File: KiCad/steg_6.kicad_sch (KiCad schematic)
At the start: 13 parts, among them U5 W65C02S, U6 LCD

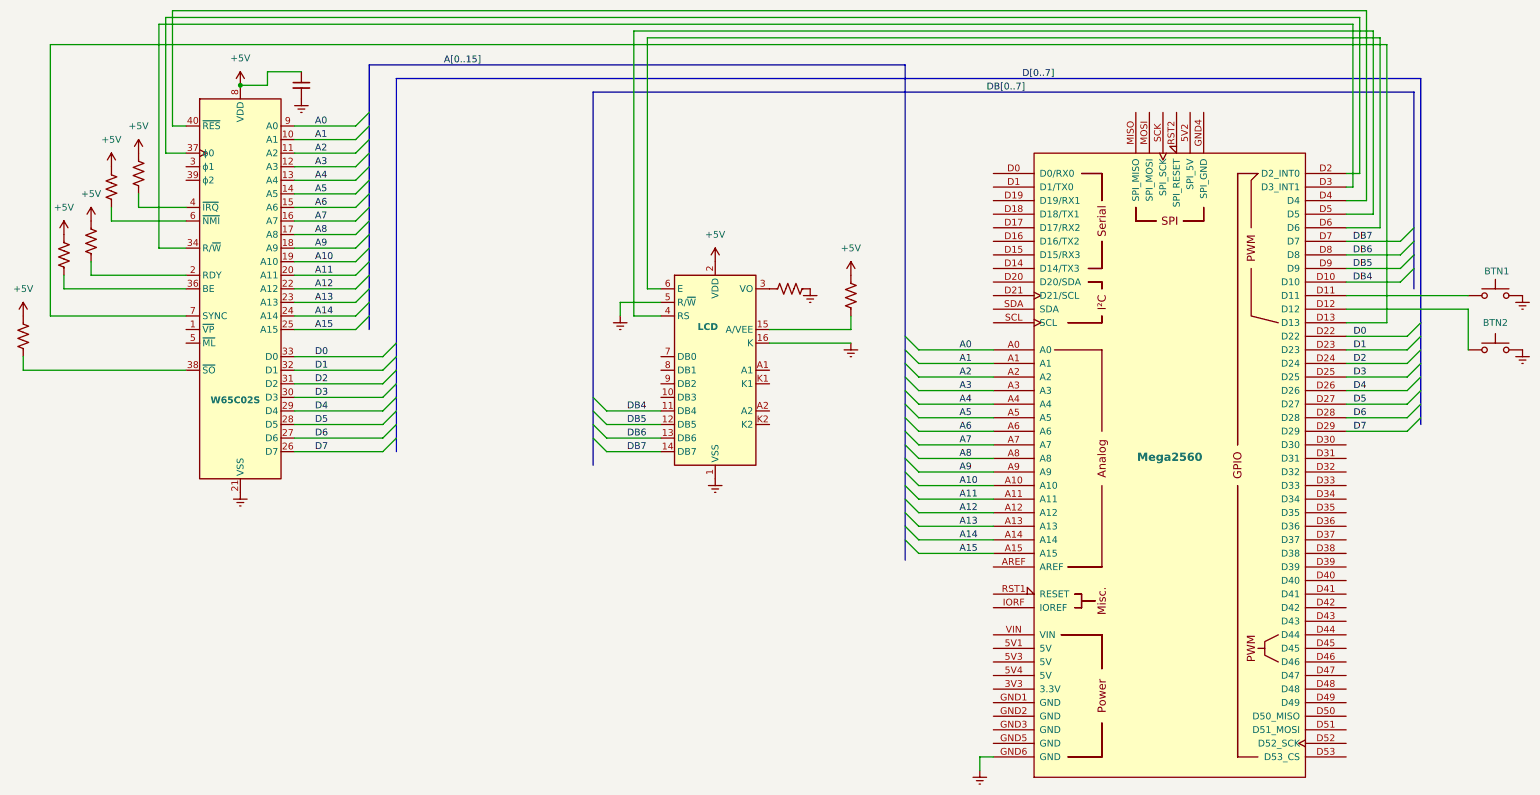
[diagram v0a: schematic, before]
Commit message: Add trim potentiometer symbol and update power symbols in schematics
- Introduced a new trim potentiometer symbol (Device:R_Potentiometer_Trim) with properties for reference, value, footprint, and simulation details.
- Updated existing power symbols for +5V and Earth, including new references and descriptions.
- Adjusted positions and properties of various components in the schematic to enhance clarity and organization.
- Updated multiple schematic images to reflect the latest changes.
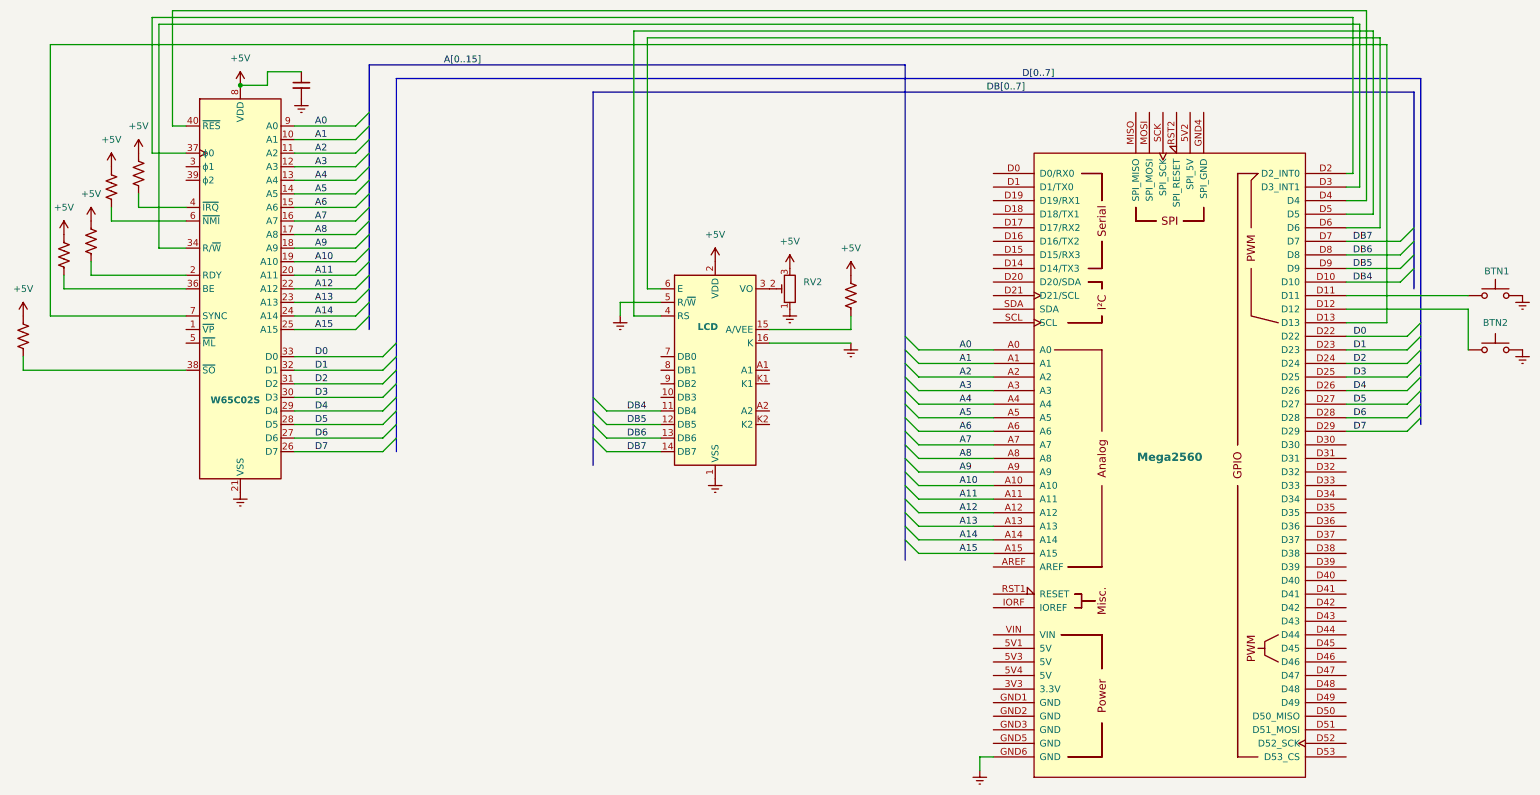
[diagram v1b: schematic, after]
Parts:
- removed R13: (no value), symbol Device:R_US
- added RV2: R_Potentiometer_Trim, symbol Device:R_Potentiometer_Trim
- R14: value (none) -> 220
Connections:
- net +5V: now also RV2.3
- net Earth: now also RV2.1
- net at U6.3 (VO): now also RV2.2
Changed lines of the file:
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@@
 	(wire
 		(pts
-			(xy 90.17 53.34) (xy 313.69 53.34)
+			(xy 87.63 53.34) (xy 312.42 53.34)
 		)
 		(stroke
@@
 	(wire
 		(pts
+			(xy 311.15 82.55) (xy 312.42 82.55)
+		)
+		(stroke
+			(width 0)
+			(type default)
+		)
+	)
+	(wire
+		(pts
 			(xy 175.26 106.68) (xy 182.88 106.68)
 		)
@@
 	(wire
 		(pts
-			(xy 88.9 54.61) (xy 312.42 54.61)
+			(xy 88.9 54.61) (xy 313.69 54.61)
 		)
 		(stroke
@@
 	(wire
 		(pts
-			(xy 90.17 53.34) (xy 90.17 78.74)
+			(xy 87.63 53.34) (xy 87.63 78.74)
 		)
 		(stroke
@@
 	(wire
 		(pts
-			(xy 90.17 78.74) (xy 93.98 78.74)
+			(xy 87.63 78.74) (xy 93.98 78.74)
 		)
 		(stroke
@@
 	(wire
 		(pts
-			(xy 312.42 85.09) (xy 311.15 85.09)
+			(xy 313.69 85.09) (xy 311.15 85.09)
 		)
 		(stroke
@@
 	(wire
 		(pts
-			(xy 312.42 54.61) (xy 312.42 85.09)
+			(xy 313.69 54.61) (xy 313.69 85.09)
 		)
 		(stroke
@@
 	(wire
 		(pts
-			(xy 313.69 53.34) (xy 313.69 82.55)
+			(xy 312.42 53.34) (xy 312.42 82.55)
 		)
 		(stroke
@@
 		(pts
 			(xy 93.98 96.52) (xy 88.9 96.52)
-		)
-		(stroke
-			(width 0)
-			(type default)
-		)
-	)
-	(wire
-		(pts
-			(xy 313.69 82.55) (xy 311.15 82.55)
 		)
 		(stroke
@@
 	)
 	(symbol
-		(lib_id "Device:R_US")
-		(at 207.01 104.14 90)
+		(lib_id "power:Earth")
+		(at 207.01 107.95 0)
 		(unit 1)
 		(body_style 1)
@@
 		(in_pos_files yes)
 		(dnp no)
-		(property "Reference" "R13"
-			(at 205.7399 101.6 90)
-			(hide yes)
-			(show_name no)
-			(do_not_autoplace no)
-			(effects
-				(font
-					(size 1.27 1.27)
-				)
-				(justify left)
-			)
-		)
-		(property "Value" ""
-			(at 208.2799 101.6 0)
-			(show_name no)
-			(do_not_autoplace no)
-			(effects
-				(font
-					(size 1.27 1.27)
-				)
-				(justify left)
+		(fields_autoplaced yes)
+		(property "Reference" "#PWR060"
+			(at 207.01 114.3 0)
+			(hide yes)
+			(show_name no)
+			(do_not_autoplace no)
+			(effects
+				(font
+					(size 1.27 1.27)
+				)
+			)
+		)
+		(property "Value" "Earth"
+			(at 207.01 113.03 0)
+			(hide yes)
+			(show_name no)
+			(do_not_autoplace no)
+			(effects
+				(font
+					(size 1.27 1.27)
+				)
 			)
 		)
 		(property "Footprint" ""
-			(at 207.264 103.124 90)
+			(at 207.01 107.95 0)
 			(hide yes)
 			(show_name no)
@@
 		)
 		(property "Datasheet" ""
-			(at 207.01 104.14 0)
-			(hide yes)
-			(show_name no)
-			(do_not_autoplace no)
-			(effects
-				(font
-					(size 1.27 1.27)
-				)
-			)
-		)
-		(property "Description" "Resistor, US symbol"
-			(at 207.01 104.14 0)
+			(at 207.01 107.95 0)
+			(hide yes)
+			(show_name no)
+			(do_not_autoplace no)
+			(effects
+				(font
+					(size 1.27 1.27)
+				)
+			)
+		)
+		(property "Description" "Power symbol creates a global label with name \"Earth\""
+			(at 207.01 107.95 0)
 			(hide yes)
 			(show_name no)
@@
 		)
 		(pin "1"
-		)
-		(pin "2"
 		)
 		(instances
 			(project "6502.smutje.se"
 				(path "/2f94eef7-ba60-41d7-948a-a400f17ff44b"
-					(reference "R13")
+					(reference "#PWR060")
 					(unit 1)
 				)
@@
 	)
 	(symbol
-		(lib_id "power:Earth")
-		(at 210.82 104.14 0)
-		(unit 1)
-		(body_style 1)
-		(exclude_from_sim no)
-		(in_bom yes)
-		(on_board yes)
-		(in_pos_files yes)
-		(dnp no)
-		(fields_autoplaced yes)
-		(property "Reference" "#PWR032"
-			(at 210.82 110.49 0)
-			(hide yes)
-			(show_name no)
-			(do_not_autoplace no)
-			(effects
-				(font
-					(size 1.27 1.27)
-				)
-			)
-		)
-		(property "Value" "Earth"
-			(at 210.82 109.22 0)
-			(hide yes)
-			(show_name no)
-			(do_not_autoplace no)
-			(effects
-				(font
-					(size 1.27 1.27)
-				)
-			)
-		)
-		(property "Footprint" ""
-			(at 210.82 104.14 0)
-			(hide yes)
-			(show_name no)
-			(do_not_autoplace no)
-			(effects
-				(font
-					(size 1.27 1.27)
-				)
-			)
-		)
-		(property "Datasheet" ""
-			(at 210.82 104.14 0)
-			(hide yes)
-			(show_name no)
-			(do_not_autoplace no)
-			(effects
-				(font
-					(size 1.27 1.27)
-				)
-			)
-		)
-		(property "Description" "Power symbol creates a global label with name \"Earth\""
-			(at 210.82 104.14 0)
-			(hide yes)
-			(show_name no)
-			(do_not_autoplace no)
-			(effects
-				(font
-					(size 1.27 1.27)
-				)
-			)
-		)
-		(pin "1"
-		)
-		(instances
-			(project "6502.smutje.se"
-				(path "/2f94eef7-ba60-41d7-948a-a400f17ff44b"
-					(reference "#PWR032")
-					(unit 1)
-				)
-			)
-		)
-	)
-	(symbol
 		(lib_id "power:+5V")
 		(at 76.2 91.44 0)
@@
 			)
 		)
-		(property "Value" ""
+		(property "Value" "220"
 			(at 220.98 106.6799 0)
+			(hide yes)
 			(show_name no)
 			(do_not_autoplace no)
@@
 	)
 	(symbol
+		(lib_id "Device:R_Potentiometer_Trim")
+		(at 207.01 104.14 180)
+		(unit 1)
+		(body_style 1)
+		(exclude_from_sim no)
+		(in_bom yes)
+		(on_board yes)
+		(in_pos_files yes)
+		(dnp no)
+		(fields_autoplaced yes)
+		(property "Reference" "RV2"
+			(at 209.55 102.8699 0)
+			(show_name no)
+			(do_not_autoplace no)
+			(effects
+				(font
+					(size 1.27 1.27)
+				)
+				(justify right)
+			)
+		)
+		(property "Value" "R_Potentiometer_Trim"
+			(at 209.55 105.4099 0)
+			(hide yes)
+			(show_name no)
+			(do_not_autoplace no)
+			(effects
+				(font
+					(size 1.27 1.27)
+				)
+				(justify right)
+			)
+		)
+		(property "Footprint" ""
+			(at 207.01 104.14 0)
+			(hide yes)
+			(show_name no)
+			(do_not_autoplace no)
+			(effects
+				(font
+					(size 1.27 1.27)
+				)
+			)
+		)
+		(property "Datasheet" ""
+			(at 207.01 104.14 0)
+			(hide yes)
+			(show_name no)
+			(do_not_autoplace no)
+			(effects
+				(font
+					(size 1.27 1.27)
+				)
+			)
+		)
+		(property "Description" "Trim-potentiometer"
+			(at 207.01 104.14 0)
+			(hide yes)
+			(show_name no)
+			(do_not_autoplace no)
+			(effects
+				(font
+					(size 1.27 1.27)
+				)
+			)
+		)
+		(property "Sim.Device" "R"
+			(at 207.01 104.14 0)
+			(hide yes)
+			(show_name no)
+			(do_not_autoplace no)
+			(effects
+				(font
+					(size 1.27 1.27)
+				)
+			)
+		)
+		(property "Sim.Type" "POT"
+			(at 207.01 104.14 0)
+			(hide yes)
+			(show_name no)
+			(do_not_autoplace no)
+			(effects
+				(font
+					(size 1.27 1.27)
+				)
+			)
+		)
+		(property "Sim.Pins" "1=r0 2=wiper 3=r1"
+			(at 207.01 104.14 0)
+			(hide yes)
+			(show_name no)
+			(do_not_autoplace no)
+			(effects
+				(font
+					(size 1.27 1.27)
+				)
+			)
+		)
+		(pin "3"
+		)
+		(pin "2"
+		)
+		(pin "1"
+		)
+		(instances
+			(project "6502.smutje.se"
+				(path "/2f94eef7-ba60-41d7-948a-a400f17ff44b"
+					(reference "RV2")
+					(unit 1)
+				)
+			)
+		)
+	)
+	(symbol
 		(lib_id "power:+5V")
 		(at 63.5 109.22 0)
@@
 					(unit 1)
 				)
+			)
+		)
+	)
+	(symbol
+		(lib_id "power:+5V")
+		(at 207.01 100.33 0)
+		(unit 1)
+		(body_style 1)
+		(exclude_from_sim no)
+		(in_bom yes)
+		(on_board yes)
+		(in_pos_files yes)
+		(dnp no)
+		(fields_autoplaced yes)
+		(property "Reference" "#PWR059"
+			(at 207.01 104.14 0)
+			(hide yes)
+			(show_name no)
+			(do_not_autoplace no)
+			(effects
+				(font
+					(size 1.27 1.27)
+				)
+			)
+		)
+		(property "Value" "+5V"
+			(at 207.01 95.25 0)
+			(show_name no)
+			(do_not_autoplace no)
+			(effects
+				(font
+					(size 1.27 1.27)
+				)
+			)
+		)
+		(property "Footprint" ""
+			(at 207.01 100.33 0)
+			(hide yes)
+			(show_name no)
+			(do_not_autoplace no)
+			(effects
+				(font
+					(size 1.27 1.27)
+				)
+			)
+		)
+		(property "Datasheet" ""
+			(at 207.01 100.33 0)
+			(hide yes)
+			(show_name no)
+			(do_not_autoplace no)
+			(effects
+				(font
+					(size 1.27 1.27)
+				)
+			)
+		)
+		(property "Description" "Power symbol creates a global label with name \"+5V\""
+			(at 207.01 100.33 0)
+			(hide yes)
+			(show_name no)
+			(do_not_autoplace no)
+			(effects
+				(font
+					(size 1.27 1.27)
+				)
+			)
+		)
+		(pin "1"
+		)
+		(instances
+			(project "6502.smutje.se"
+				(path "/2f94eef7-ba60-41d7-948a-a400f17ff44b"
+					(reference "#PWR059")
+					(unit 1)
+				)
